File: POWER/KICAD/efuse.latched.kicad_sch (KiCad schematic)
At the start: 6 parts

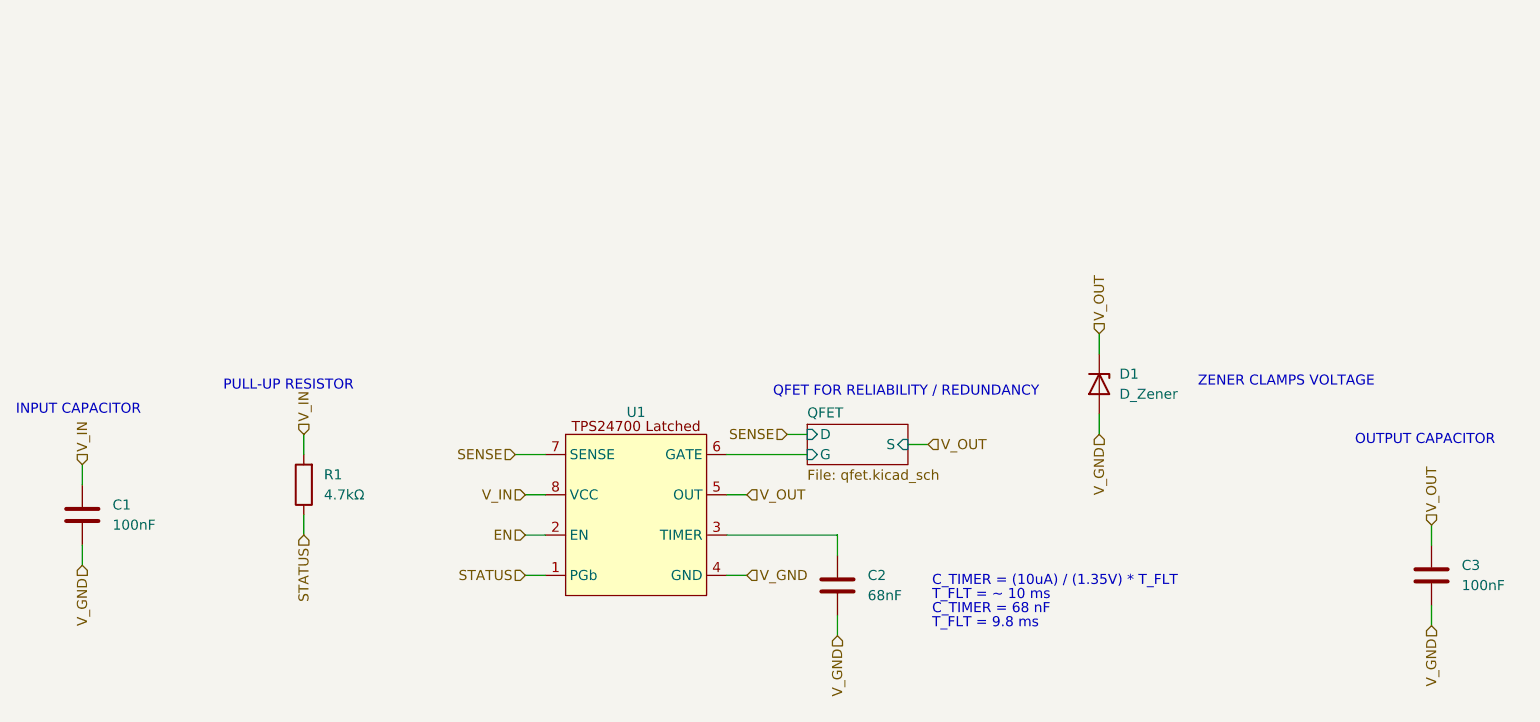
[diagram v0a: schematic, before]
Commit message: Updated Power Schematic / Kicad
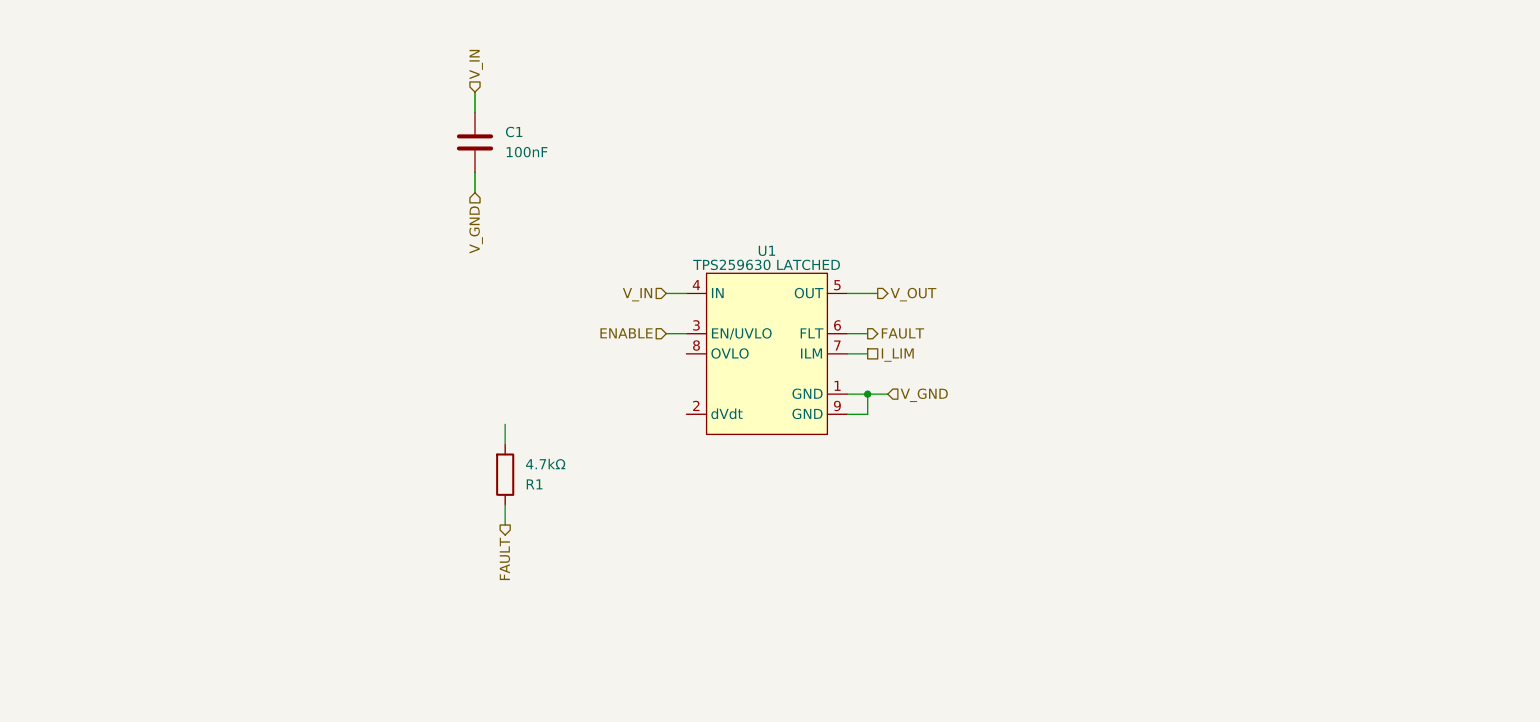
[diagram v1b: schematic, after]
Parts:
- removed C2: 68nF, symbol Device:C
- removed C3: 100nF, symbol Device:C
- removed D1: D_Zener, symbol Device:D_Zener
- removed U1: ~, symbol CUBESAT:TPS24700
- added U1: TPS259630 LATCHED, symbol CUBESAT:TPS259630
- C1: footprint (none) -> Capacitor_SMD:C_0603_1608Metric
- R1: footprint (none) -> Resistor_SMD:R_0603_1608Metric
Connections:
- net V_GND: now also U1.1 (GND), U1.9 (GND)
- net V_IN: now also U1.4 (IN); no longer R1.2
- net V_OUT: now also U1.5 (OUT)
- net STATUS renamed FAULT
- net FAULT: now also U1.6 (FLT)
- new net ENABLE: U1.3 (EN/UVLO)
- new net I_LIM: U1.7 (ILM)
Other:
- removed sheet QFET
- note removed: "C_TIMER = (10uA) / (1.35V) * T_FLT"
- note removed: "C_TIMER = 68 nF"
- note removed: "INPUT CAPACITOR"
- note removed: "OUTPUT CAPACITOR"
- note removed: "PULL-UP RESISTOR"
- note removed: "QFET FOR RELIABILITY / REDUNDANCY"
- note removed: "T_FLT = 9.8 ms"
- note removed: "T_FLT = ~ 10 ms"
- note removed: "ZENER CLAMPS VOLTAGE"

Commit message: schematic design
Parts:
- removed C1: 100nF, Capacitor_SMD:C_0603_1608Metric, symbol Device:C
- removed R1: 4.7kΩ, Resistor_SMD:R_0603_1608Metric, symbol Device:R
- removed U1: TPS259630 LATCHED, symbol CUBESAT:TPS259630
- added C?: 4.7nF, Capacitor_SMD:C_0603_1608Metric, symbol Device:C
- added R? (x2): 4.7kΩ, symbol Device:R
- added R?: 30kΩ, symbol Device:R
- added U?: TPS259474L, symbol CUBESAT:TPS259474LRPW
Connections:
- net ENABLE: now also R?.1, R?.2, U?.1 (EN/UVLO)
- net I_LIM: now also U?.9 (ILM)
- net V_GND: now also R?.2, U?.8 (GND)
- net V_IN: now also R?.1, U?.5 (IN)
- net V_OUT: now also U?.6 (OUT)
- new net STATUS: U?.3 (PG)
- new net UVLO: R?.1, R?.2, U?.2 (OVLO)
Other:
- note added: "CURRENT LIMIT R = 3334 / I"
- note added: "OV: 11 V UV: 5.6 V"
